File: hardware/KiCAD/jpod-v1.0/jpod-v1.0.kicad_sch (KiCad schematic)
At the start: 1 part, among them U1 ESP32-WROVER-E-N16R8

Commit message: kicad files
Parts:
- added R1, R2, R3, R4: 10K, Resistor_SMD:R_0603_1608Metric, symbol Device:R
- added SW1, SW2, SW3, SW4, SW5: TL3342F160QG_TR, jpod_footprints:SW_TL3342F160QG_TR, symbol jpod:TL3342F160QG_TR
- U1: footprint ESP32-WROVER-E-N16R8:ESP32-WROVER-E_EXP -> jpod_footprints:ESP32-WROVER-E_EXP
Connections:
- net GND: now reaches U1.1 (GND_2)
- net GND: now also SW1.3, SW1.4, SW2.3, SW2.4, SW3.3, SW3.4, SW4.3, SW4.4, SW5.3, SW5.4
- net 3V3: now reaches U1.2 (3V3)
- net 3V3: now also U1.8 (IO32), R1.2, R2.2, R3.2, R4.2, SW3.1, SW3.2
- net btn_left: now reaches U1.4 (SENSOR_VP)
- net btn_left: now also R4.1, SW2.1, SW2.2
- net btn_right: now reaches U1.5 (SENSOR_VN)
- net btn_right: now also R2.1, SW5.1, SW5.2
- net btn_up: now reaches U1.6 (IO34)
- net btn_up: now also R1.1, SW1.1, SW1.2
- net btn_down: now reaches U1.7 (IO35)
- net btn_down: now also R3.1, SW4.1, SW4.2
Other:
- moved on the sheet: U1

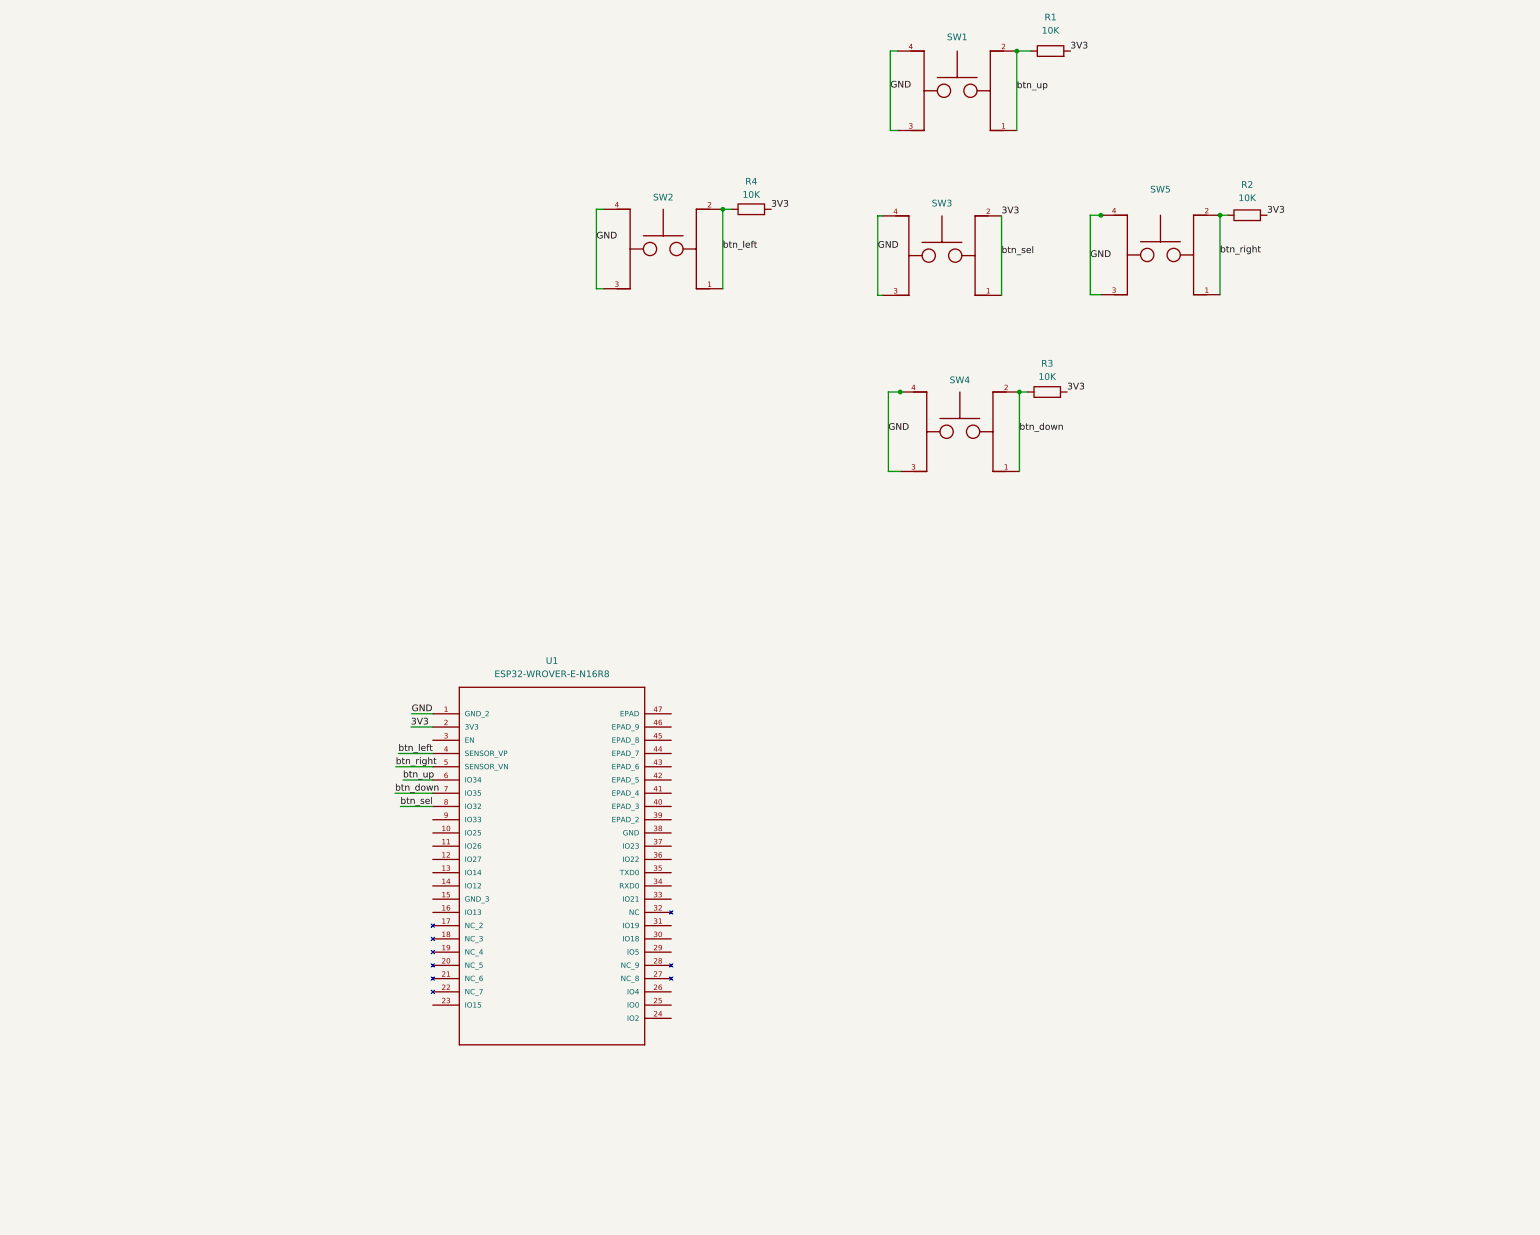
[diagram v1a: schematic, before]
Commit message: dm3at sd card holder added to library. Schematic updated to add decoupling caps and SPI bus for SD card holder
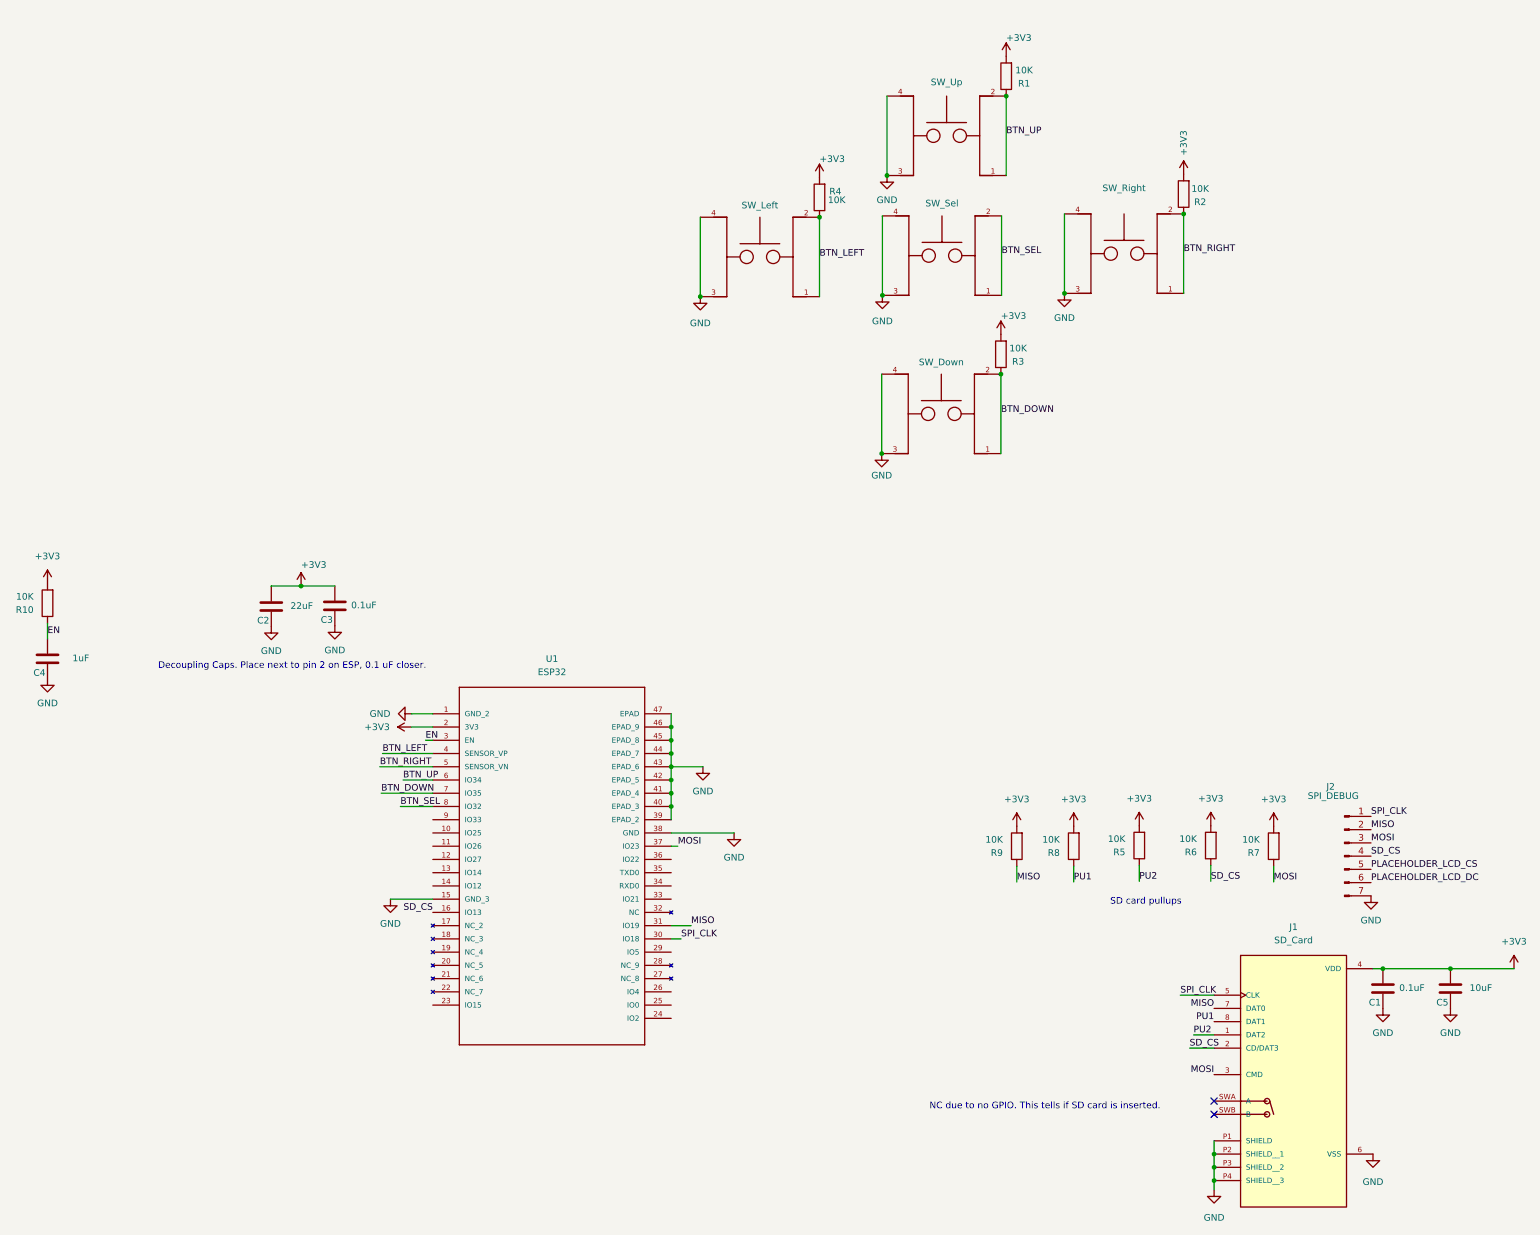
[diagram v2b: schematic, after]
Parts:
- added C1, C3: 0.1uF, Capacitor_SMD:C_0603_1608Metric, symbol Device:C
- added C2: 22uF, Capacitor_SMD:C_0603_1608Metric, symbol Device:C
- added C4: 1uF, Capacitor_SMD:C_0603_1608Metric, symbol Device:C
- added C5: 10uF, Capacitor_SMD:C_0603_1608Metric, symbol Device:C
- added J1: SD_Card, jpod_footprints:HRS_DM3AT-SF-PEJM5, symbol jpod:DM3AT-SF-PEJM5
- added J2: SPI_DEBUG, Connector_PinHeader_2.54mm:PinHeader_1x07_P2.54mm_Vertical, symbol Connector:Conn_01x07_Pin
- added R10, R5, R6, R7, R8, R9: 10K, Resistor_SMD:R_0603_1608Metric, symbol Device:R
- U1: value ESP32-WROVER-E-N16R8 -> ESP32
- renumbered SW4 to SW_Down, SW2 to SW_Left, SW5 to SW_Right, SW3 to SW_Sel, SW1 to SW_Up
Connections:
- net GND: now also U1.15 (GND_3), U1.38 (GND), U1.39 (EPAD_2), U1.40 (EPAD_3), U1.41 (EPAD_4), U1.42 (EPAD_5), U1.43 (EPAD_6), U1.44 (EPAD_7), U1.45 (EPAD_8), U1.46 (EPAD_9), U1.47 (EPAD), C1.1, C2.1, C3.1, C4.1, C5.1, J1.6 (VSS), J1.P1 (SHIELD), J1.P2 (SHIELD__1), J1.P3 (SHIELD__2), J1.P4 (SHIELD__3), J2.7 (Pin_7)
- net SD_CS: now reaches U1.16 (IO13)
- net SD_CS: now also J1.2 (CD/DAT3), J2.4 (Pin_4), R6.1
- net EN: now reaches U1.3 (EN)
- net EN: now also C4.2, R10.1
- net SPI_CLK: now reaches U1.30 (IO18)
- net SPI_CLK: now also J1.5 (CLK), J2.1 (Pin_1)
- net MISO: now reaches U1.31 (IO19)
- net MISO: now also J1.7 (DAT0), J2.2 (Pin_2), R9.1
- net MOSI: now reaches U1.37 (IO23)
- net MOSI: now also J1.3 (CMD), J2.3 (Pin_3), R7.1
- net 3V3 renamed +3V3
- net +3V3: now also C1.2, C2.2, C3.2, C5.2, J1.4 (VDD), R10.2, R5.2, R6.2, R7.2, R8.2, R9.2; no longer SW_Sel.1, SW_Sel.2, U1.8 (IO32)
- net btn_down renamed BTN_DOWN
- net btn_left renamed BTN_LEFT
- net btn_right renamed BTN_RIGHT
- net btn_up renamed BTN_UP
- new net BTN_SEL: SW_Sel.1, SW_Sel.2, U1.8 (IO32)
- new net PLACEHOLDER_LCD_CS: J2.5 (Pin_5)
- new net PLACEHOLDER_LCD_DC: J2.6 (Pin_6)
- new net PU1: J1.8 (DAT1), R8.1
- new net PU2: J1.1 (DAT2), R5.1
- no-connect marks 0 -> 2
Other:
- note added: "Decoupling Caps. Place next to pin 2 on ESP, 0.1 uF closer."
- note added: "NC due to no GPIO. This tells if SD card is inserted."
- note added: "SD card pullups"
- moved on the sheet: R1, R2, R3, SW_Down, SW_Left, SW_Right, SW_Up

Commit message: work on display
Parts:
- added J3: LCD_HEADER, Connector_FFC-FPC:Hirose_FH12-22S-0.5SH_1x22-1MP_P0.50mm_Horizontal, symbol Connector:Conn_01x22_Pin
- added Q1: AO3400A, Package_TO_SOT_SMD:SOT-23, symbol Transistor_FET:AO3400A
- added R11: 100, Resistor_SMD:R_0603_1608Metric, symbol Device:R
- added R12: 100K, Resistor_SMD:R_0603_1608Metric, symbol Device:R
- added R13: 6.8, Resistor_SMD:R_0603_1608Metric, symbol Device:R
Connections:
- net +3V3: now also R13.2
- net GND: now also J3.10 (Pin_10), J3.11 (Pin_11), J3.12 (Pin_12), J3.13 (Pin_13), J3.14 (Pin_14), J3.7 (Pin_7), J3.8 (Pin_8), J3.9 (Pin_9), Q1.2 (S), R12.1
- net BACKLIGHT: now reaches U1.26 (IO4)
- net BACKLIGHT: now also R11.2
- new net: Q1.1 (G), R11.1, R12.2
- new net: J3.1 (Pin_1), R13.1
- new net CAT: J3.2 (Pin_2), Q1.3 (D)

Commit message: completed lcd header
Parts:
- added C6: 0.1uF, Capacitor_SMD:C_0603_1608Metric, symbol Device:C
- renumbered SW_Down to SW_Down1, SW_Left to SW_Left1, SW_Right to SW_Right1, SW_Sel to SW_Sel1, SW_Up to SW_Up1
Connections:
- net +3V3: now also J3.15 (Pin_15), J3.3 (Pin_3), J3.4 (Pin_4), J3.6 (Pin_6), C6.2
- net EN: now also J3.20 (Pin_20)
- net GND: now also J3.22 (Pin_22), J3.5 (Pin_5), C6.1
- net MOSI: now also J3.21 (Pin_21)
- net SPI_CLK: now also J3.17 (Pin_17)
- net LCD_DC: now reaches U1.12 (IO27)
- net LCD_DC: now also J3.16 (Pin_16)
- net LCD_CS: now reaches U1.29 (IO5)
- net LCD_CS: now also J3.18 (Pin_18)
- no-connect marks 2 -> 3
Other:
- note added: "IM pins: 0110 for 4-line 8bit serial I/F 0 already set. 3-5 = 110"
- moved on the sheet: Q1, R11, R12

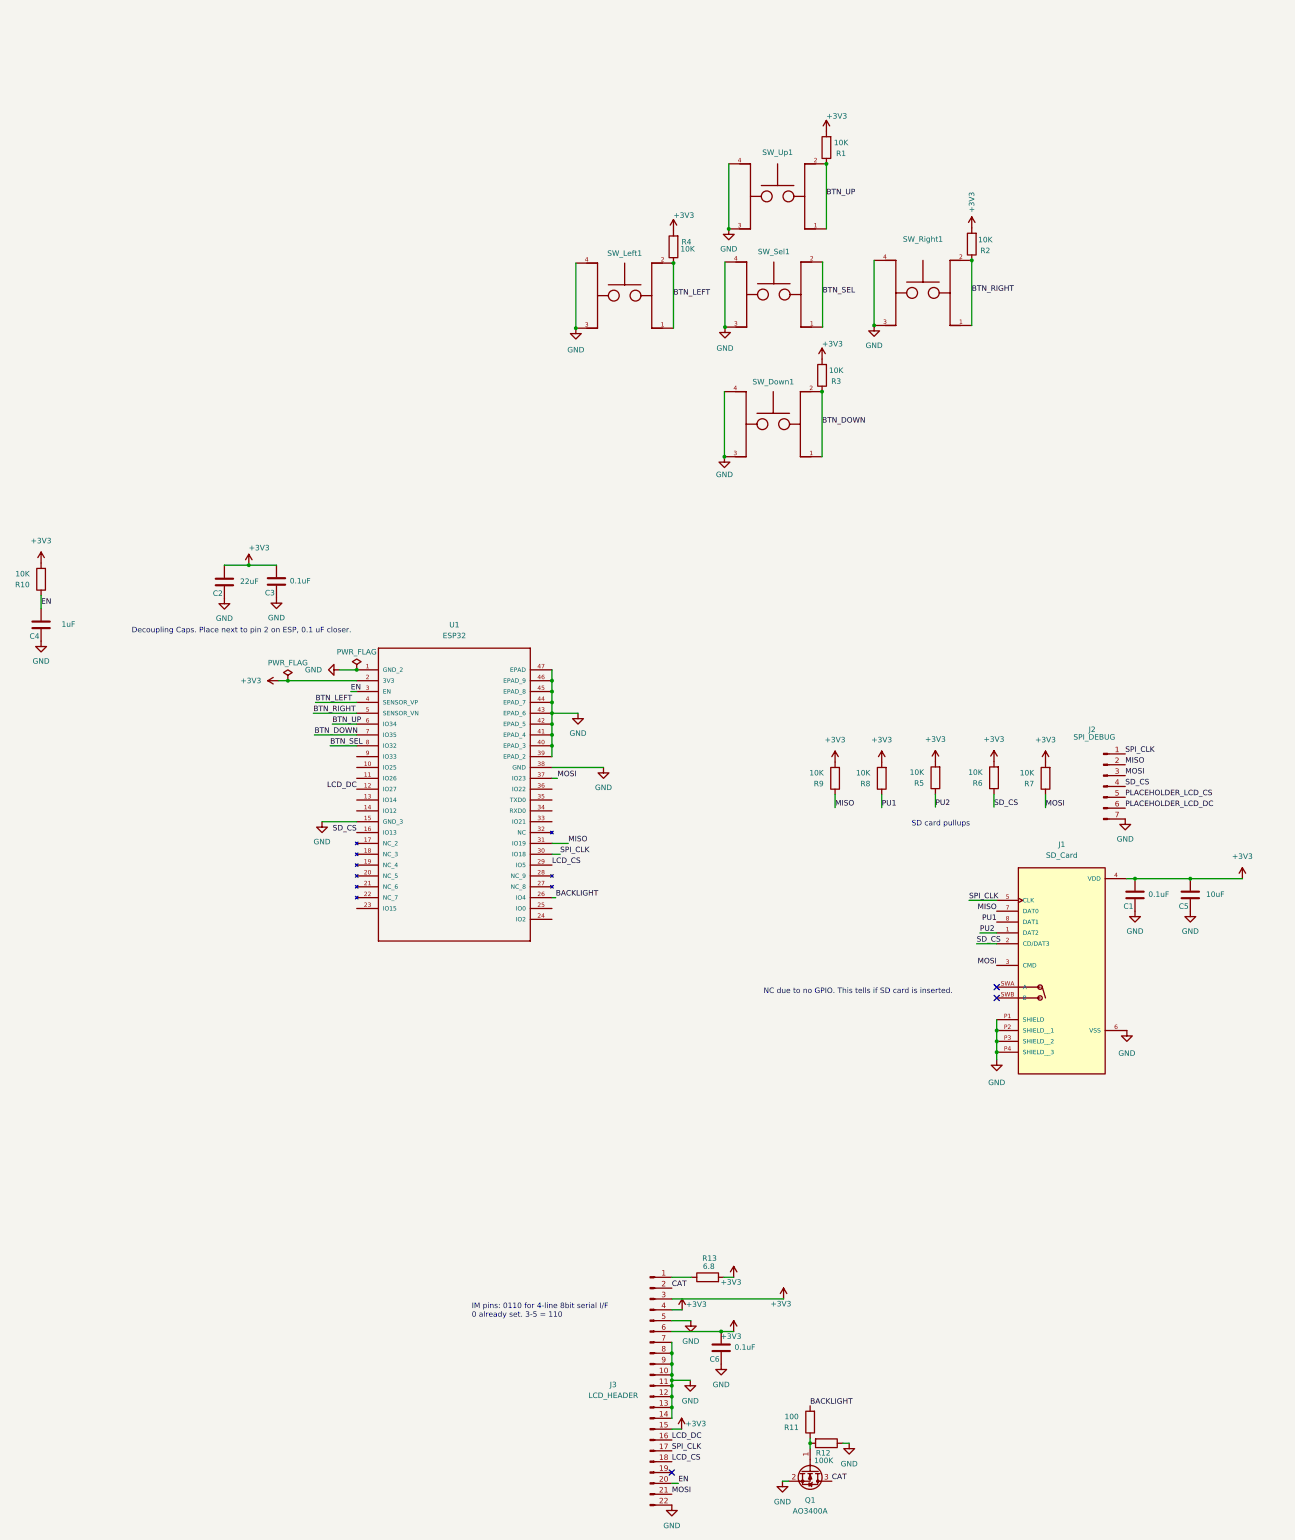
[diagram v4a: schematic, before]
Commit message: schematic cleanup and notes
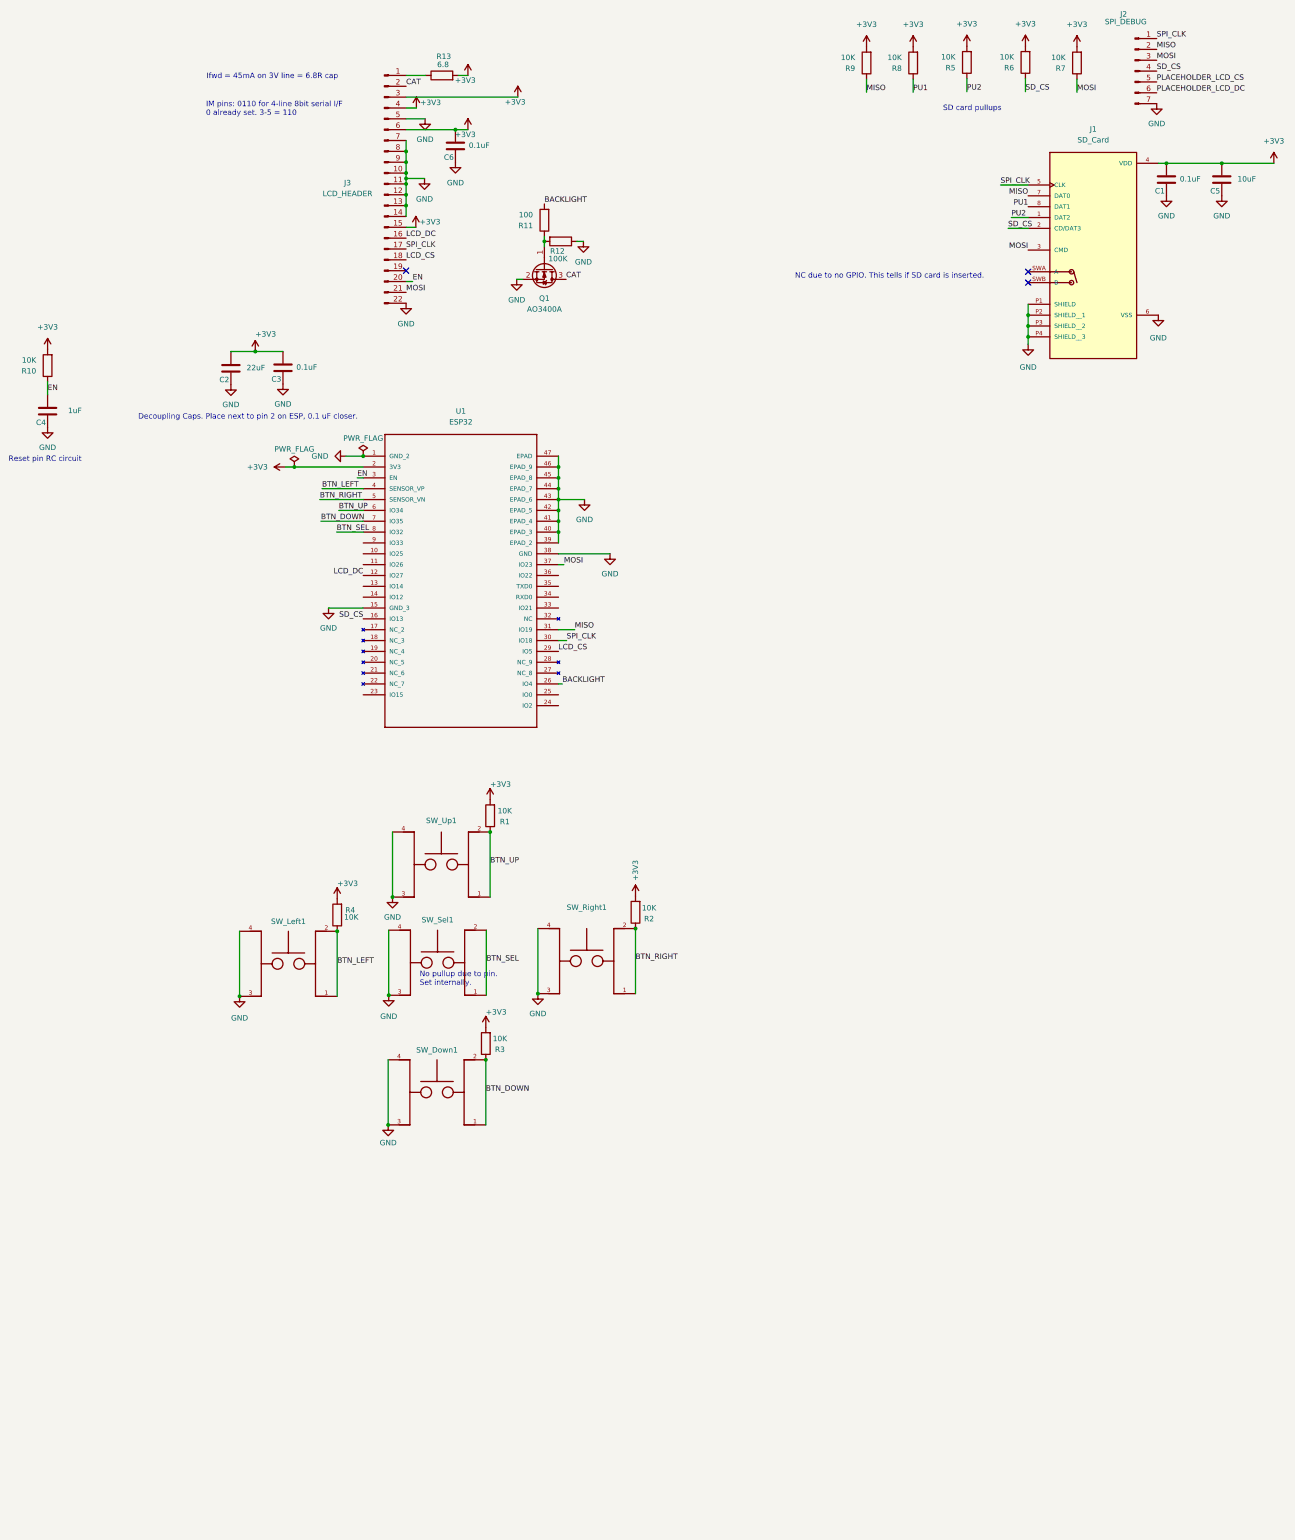
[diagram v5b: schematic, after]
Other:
- note added: "Ifwd = 45mA on 3V line = 6.8R cap"
- note added: "No pullup due to pin. Set internally."
- note added: "Reset pin RC circuit"
- moved on the sheet: C1, C2, C3, C4, C5, C6, J1, J2, J3, Q1, R1, R10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
